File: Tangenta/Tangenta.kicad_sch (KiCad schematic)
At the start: 9 parts

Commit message: Improving SDcard placement and routing
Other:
- note added: "GPIOs/IOs CMOS (Flash) FANs Reset/Power pins and buttons CR2032 & RTC"
- note removed: "GPIOs/IOs CMOS (Flash) FANs Reset/Power pins and buttons CR2032, RTC & Battery"
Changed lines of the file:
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@@
     (stroke (width 0) (type default))
   )
-  (bus (pts (xy 207.01 210.185) (xy 401.955 210.185))
+  (bus (pts (xy 207.01 213.36) (xy 401.955 213.36))
     (stroke (width 0) (type default))
   )
@@
     (stroke (width 0) (type default))
   )
-  (bus (pts (xy 207.01 205.105) (xy 207.01 210.185))
+  (bus (pts (xy 207.01 205.105) (xy 207.01 213.36))
     (stroke (width 0) (type default))
   )
@@
     (stroke (width 0) (type default))
   )
-  (bus (pts (xy 401.955 210.185) (xy 401.955 125.73))
+  (bus (pts (xy 401.955 213.36) (xy 401.955 125.73))
     (stroke (width 0) (type default))
   )
@@
     (stroke (width 0) (type default))
   )
-  (text "GPIOs/IOs\n\nCMOS (Flash)\n\nFANs\n\nReset/Power pins\nand buttons\n\nCR2032, RTC & Battery"
+  (text "GPIOs/IOs\n\nCMOS (Flash)\n\nFANs\n\nReset/Power pins\nand buttons\n\nCR2032 & RTC"
     (at -100.965 160.655 0)
     (effects (font (size 5 5)) (justify left bottom))

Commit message: RTC continued...
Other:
- added sheet RTC (RTC.kicad_sch)
- note added: "GPIOs/IOs CMOS (Flash) FANs Reset/Power pins and buttons"
- note removed: "GPIOs/IOs CMOS (Flash) FANs Reset/Power pins and buttons CR2032 & RTC"
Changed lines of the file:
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@@
   (junction (at 278.765 150.495) (diameter 0) (color 0 0 0 0)
+  )
+  (junction (at 207.01 213.36) (diameter 0) (color 0 0 0 0)
   )
   (junction (at 207.01 205.105) (diameter 0) (color 0 0 0 0)
@@
     (stroke (width 0) (type default))
   )
+  (wire (pts (xy 241.3 225.425) (xy 254.635 225.425))
+    (stroke (width 0) (type default))
+  )
   (wire (pts (xy 254.635 133.35) (xy 267.97 133.35))
     (stroke (width 0) (type default))
@@
     (stroke (width 0) (type default))
   )
+  (bus (pts (xy 207.01 231.14) (xy 207.01 213.36))
+    (stroke (width 0) (type default))
+  )
   (wire (pts (xy 355.6 150.495) (xy 368.935 150.495))
     (stroke (width 0) (type default))
   )
+  (wire (pts (xy 241.3 222.885) (xy 254.635 222.885))
+    (stroke (width 0) (type default))
+  )
   (wire (pts (xy 333.375 187.325) (xy 346.71 187.325))
     (stroke (width 0) (type default))
@@
     (stroke (width 0) (type default))
   )
+  (bus (pts (xy 214.63 231.14) (xy 207.01 231.14))
+    (stroke (width 0) (type default))
+  )
   (bus (pts (xy 401.955 213.36) (xy 401.955 125.73))
     (stroke (width 0) (type default))
@@
     (stroke (width 0) (type default))
   )
-  (text "GPIOs/IOs\n\nCMOS (Flash)\n\nFANs\n\nReset/Power pins\nand buttons\n\nCR2032 & RTC"
+  (text "GPIOs/IOs\n\nCMOS (Flash)\n\nFANs\n\nReset/Power pins\nand buttons"
     (at -100.965 160.655 0)
     (effects (font (size 5 5)) (justify left bottom))
@@
     (effects (font (size 1.27 1.27)) (justify right bottom))
   )
+  (label "GND" (at 254.635 225.425 180) (fields_autoplaced)
+    (effects (font (size 1.27 1.27)) (justify right bottom))
+  )
   (label "GND" (at 402.59 52.07 180) (fields_autoplaced)
     (effects (font (size 1.27 1.27)) (justify right bottom))
@@
   )
   (label "GND" (at 346.71 147.955 180) (fields_autoplaced)
+    (effects (font (size 1.27 1.27)) (justify right bottom))
+  )
+  (label "3V3" (at 254.635 222.885 180) (fields_autoplaced)
     (effects (font (size 1.27 1.27)) (justify right bottom))
   )
@@
       )
     )
+  )
+  (sheet (at 214.63 219.71) (size 26.67 17.145) (fields_autoplaced)
+    (stroke (width 0.1524) (type solid))
+    (fill (color 0 0 0 0.0000))
+    (property "Sheetname" "RTC" (at 214.63 218.9984 0)
+      (effects (font (size 1.27 1.27)) (justify left bottom))
+    )
+    (property "Sheetfile" "RTC.kicad_sch" (at 214.63 237.4396 0)
+      (effects (font (size 1.27 1.27)) (justify left top))
+    )
+    (pin "SMBUS{SCL SDA}" input (at 214.63 231.14 180)
+      (effects (font (size 1.27 1.27)) (justify left))
+    )
+    (pin "3V3" input (at 241.3 222.885 0)
+      (effects (font (size 1.27 1.27)) (justify right))
+    )
+    (pin "GND" bidirectional (at 241.3 225.425 0)
+      (effects (font (size 1.27 1.27)) (justify right))
+    )
+    (instances
+      (project "Tangenta"
+        (path "/358d1bcf-7599-4352-8c4d-baa18a5f09e6" (page "28"))
+      )
+    )

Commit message: DualCMOS
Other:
- added sheet DualCMOS (DualCMOS.kicad_sch)
- note added: "GPIOs/IOs FANs Reset/Power pins and buttons"
- note removed: "GPIOs/IOs CMOS (Flash) FANs Reset/Power pins and buttons"
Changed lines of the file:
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@@
   (junction (at 278.765 150.495) (diameter 0) (color 0 0 0 0)
+  )
+  (junction (at 207.01 231.14) (diameter 0) (color 0 0 0 0)
   )
   (junction (at 207.01 213.36) (diameter 0) (color 0 0 0 0)
@@
     (stroke (width 0) (type default))
   )
+  (wire (pts (xy 241.3 249.555) (xy 254.635 249.555))
+    (stroke (width 0) (type default))
+  )
   (bus (pts (xy 188.595 170.815) (xy 294.64 170.815))
     (stroke (width 0) (type default))
@@
     (stroke (width 0) (type default))
   )
+  (bus (pts (xy 214.63 249.555) (xy 207.01 249.555))
+    (stroke (width 0) (type default))
+  )
   (wire (pts (xy 46.355 171.45) (xy 52.705 171.45))
     (stroke (width 0) (type default))
@@
     (stroke (width 0) (type default))
   )
+  (wire (pts (xy 241.3 247.015) (xy 254.635 247.015))
+    (stroke (width 0) (type default))
+  )
   (wire (pts (xy 85.09 159.385) (xy 98.425 159.385))
     (stroke (width 0) (type default))
@@
     (stroke (width 0) (type default))
   )
+  (bus (pts (xy 207.01 249.555) (xy 207.01 231.14))
+    (stroke (width 0) (type default))
+  )
   (wire (pts (xy 254.635 135.89) (xy 267.97 135.89))
     (stroke (width 0) (type default))
@@
     (stroke (width 0) (type default))
   )
-  (text "GPIOs/IOs\n\nCMOS (Flash)\n\nFANs\n\nReset/Power pins\nand buttons"
-    (at -100.965 160.655 0)
+  (text "GPIOs/IOs\n\nFANs\n\nReset/Power pins\nand buttons" (at -100.965 160.655 0)
     (effects (font (size 5 5)) (justify left bottom))
   )
@@
   )
   (label "1V8" (at 98.425 90.805 180) (fields_autoplaced)
+    (effects (font (size 1.27 1.27)) (justify right bottom))
+  )
+  (label "GND" (at 254.635 249.555 180) (fields_autoplaced)
     (effects (font (size 1.27 1.27)) (justify right bottom))
   )
@@
   )
   (label "CHASSIS" (at 346.71 189.865 180) (fields_autoplaced)
+    (effects (font (size 1.27 1.27)) (justify right bottom))
+  )
+  (label "3V3" (at 254.635 247.015 180) (fields_autoplaced)
     (effects (font (size 1.27 1.27)) (justify right bottom))
   )
@@
       )
     )
+  )
+  (sheet (at 214.63 243.84) (size 26.67 16.51) (fields_autoplaced)
+    (stroke (width 0.1524) (type solid))
+    (fill (color 0 0 0 0.0000))
+    (property "Sheetname" "DualCMOS" (at 214.63 243.1284 0)
+      (effects (font (size 1.27 1.27)) (justify left bottom))
+    )
+    (property "Sheetfile" "DualCMOS.kicad_sch" (at 214.63 260.9346 0)
+      (effects (font (size 1.27 1.27)) (justify left top))
+    )
+    (pin "SMBUS{SCL SDA}" input (at 214.63 249.555 180)
+      (effects (font (size 1.27 1.27)) (justify left))
+    )
+    (pin "GND" bidirectional (at 241.3 249.555 0)
+      (effects (font (size 1.27 1.27)) (justify right))
+    )
+    (pin "3V3" input (at 241.3 247.015 0)
+      (effects (font (size 1.27 1.27)) (justify right))
+    )
+    (instances
+      (project "Tangenta"
+        (path "/358d1bcf-7599-4352-8c4d-baa18a5f09e6" (page "29"))
+      )
+    )

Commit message: Adding on-board PWR and RST tactile buttons.
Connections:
- no-connect marks 2 -> 0
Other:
- sheet Toradex ports: added PWR, RST; removed none
- note added: "JTAG GPIOs/IOs FANs ADC"
- note removed: "GPIOs/IOs FANs Reset/Power pins and buttons"
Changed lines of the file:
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@@
   (junction (at 207.01 205.105) (diameter 0) (color 0 0 0 0)
   )
-  (no_connect (at 295.91 31.75))
-  (no_connect (at 295.91 34.29))
   (wire (pts (xy 389.255 34.29) (xy 402.59 34.29))
     (stroke (width 0) (type default))
@@
     (stroke (width 0) (type default))
   )
+  (wire (pts (xy 188.595 31.75) (xy 300.355 31.75))
+    (stroke (width 0) (type default))
+  )
   (wire (pts (xy 107.315 24.765) (xy 93.98 24.765))
     (stroke (width 0) (type default))
@@
     (stroke (width 0) (type default))
   )
-  (wire (pts (xy 295.91 34.29) (xy 300.355 34.29))
-    (stroke (width 0) (type default))
-  )
   (wire (pts (xy 368.935 147.955) (xy 355.6 147.955))
     (stroke (width 0) (type default))
@@
     (stroke (width 0) (type default))
   )
-  (wire (pts (xy 295.91 31.75) (xy 300.355 31.75))
-    (stroke (width 0) (type default))
-  )
   (bus (pts (xy 188.595 161.29) (xy 294.64 161.29))
     (stroke (width 0) (type default))
@@
     (stroke (width 0) (type default))
   )
+  (wire (pts (xy 188.595 34.29) (xy 300.355 34.29))
+    (stroke (width 0) (type default))
+  )
   (bus (pts (xy 188.595 95.25) (xy 214.63 95.25))
     (stroke (width 0) (type default))
   )
-  (text "GPIOs/IOs\n\nFANs\n\nReset/Power pins\nand buttons" (at -100.965 160.655 0)
+  (text "JTAG\n\nGPIOs/IOs\n\nFANs\n\nADC" (at -100.965 160.655 0)
     (effects (font (size 5 5)) (justify left bottom))
   )
@@
       (effects (font (size 1.27 1.27)) (justify right))
     )
+    (pin "PWR" input (at 188.595 34.29 0)
+      (effects (font (size 1.27 1.27)) (justify right))
+    )
+    (pin "RST" input (at 188.595 31.75 0)
+      (effects (font (size 1.27 1.27)) (justify right))
+    )

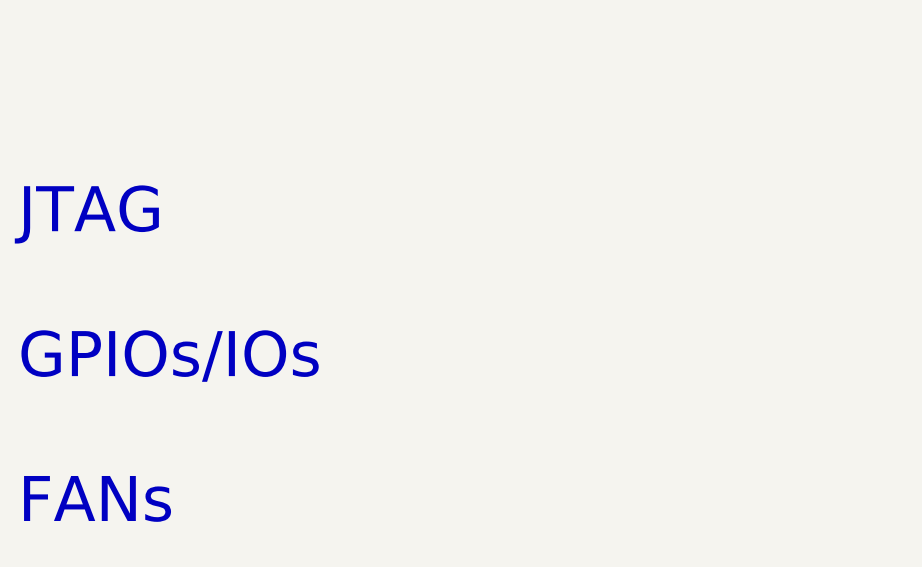
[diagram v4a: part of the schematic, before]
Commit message: Adding a hint about recovery jumper.
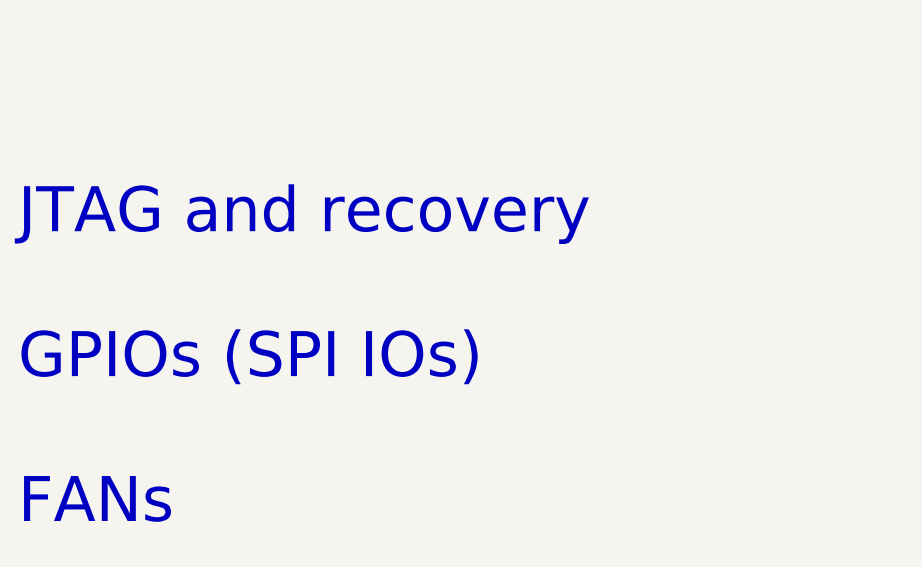
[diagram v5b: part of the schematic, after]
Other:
- note added: "JTAG and recovery GPIOs (SPI IOs) FANs ADC"
- note removed: "JTAG GPIOs/IOs FANs ADC"
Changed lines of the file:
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@@
     (stroke (width 0) (type default))
   )
-  (text "JTAG\n\nGPIOs/IOs\n\nFANs\n\nADC" (at -100.965 160.655 0)
+  (text "JTAG and recovery\n\nGPIOs (SPI IOs)\n\nFANs\n\nADC" (at -100.965 160.655 0)
     (effects (font (size 5 5)) (justify left bottom))
   )

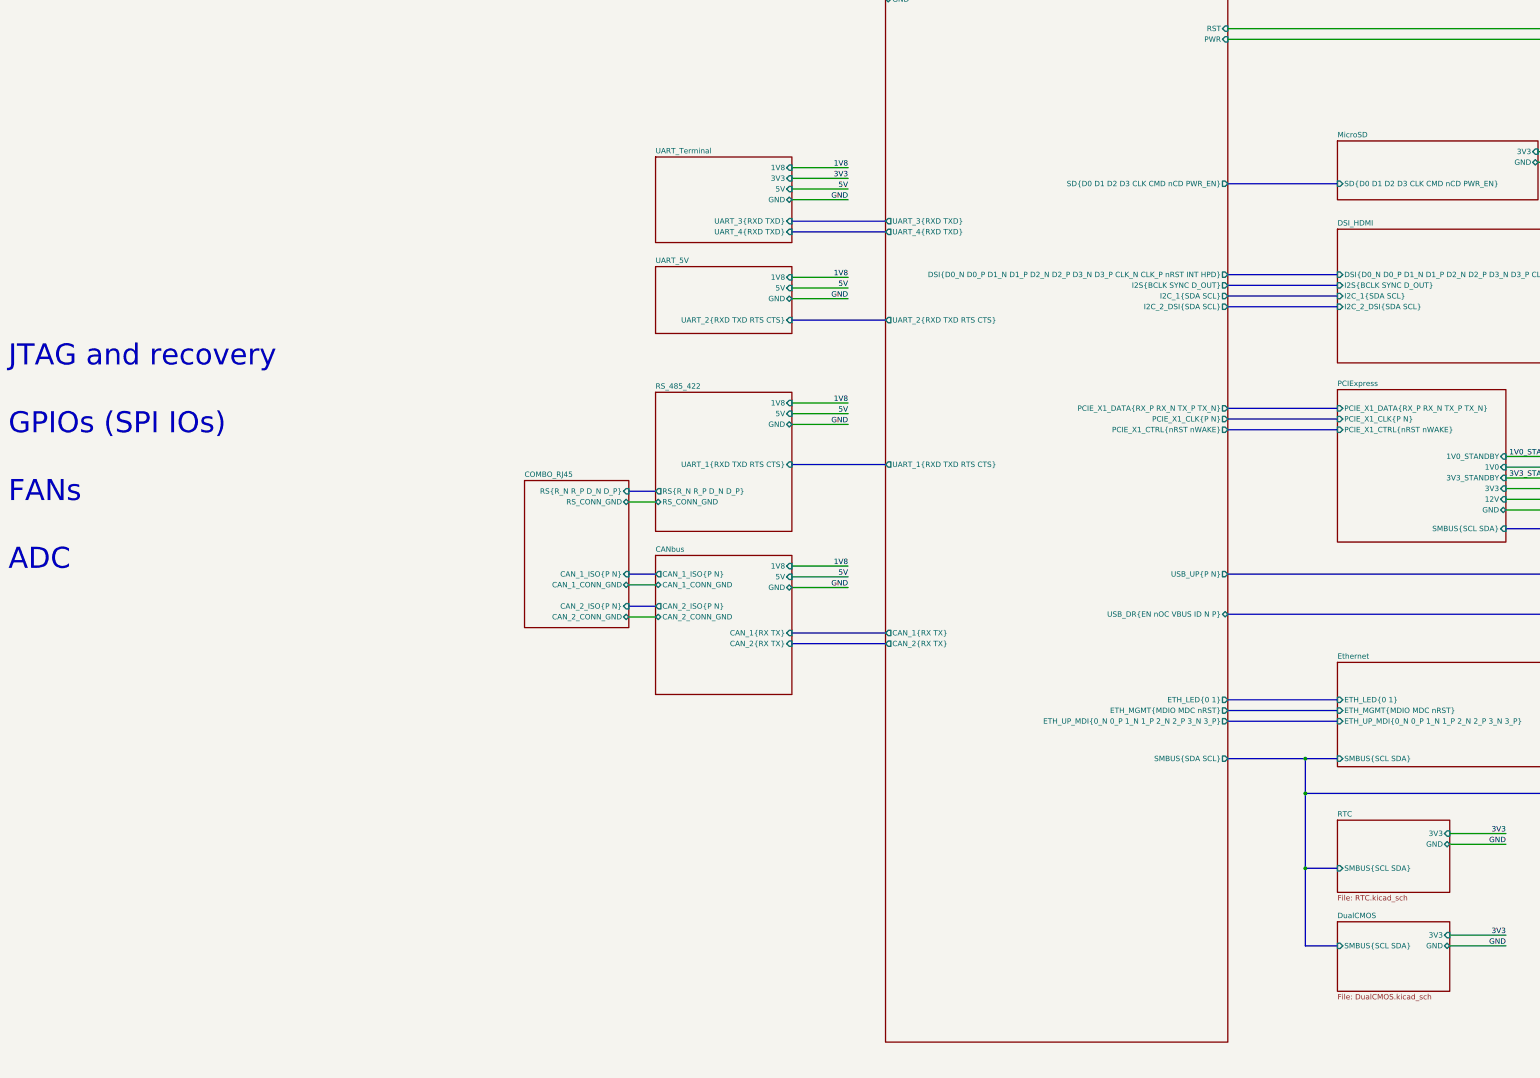
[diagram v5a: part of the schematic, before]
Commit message: Adding JTAG.
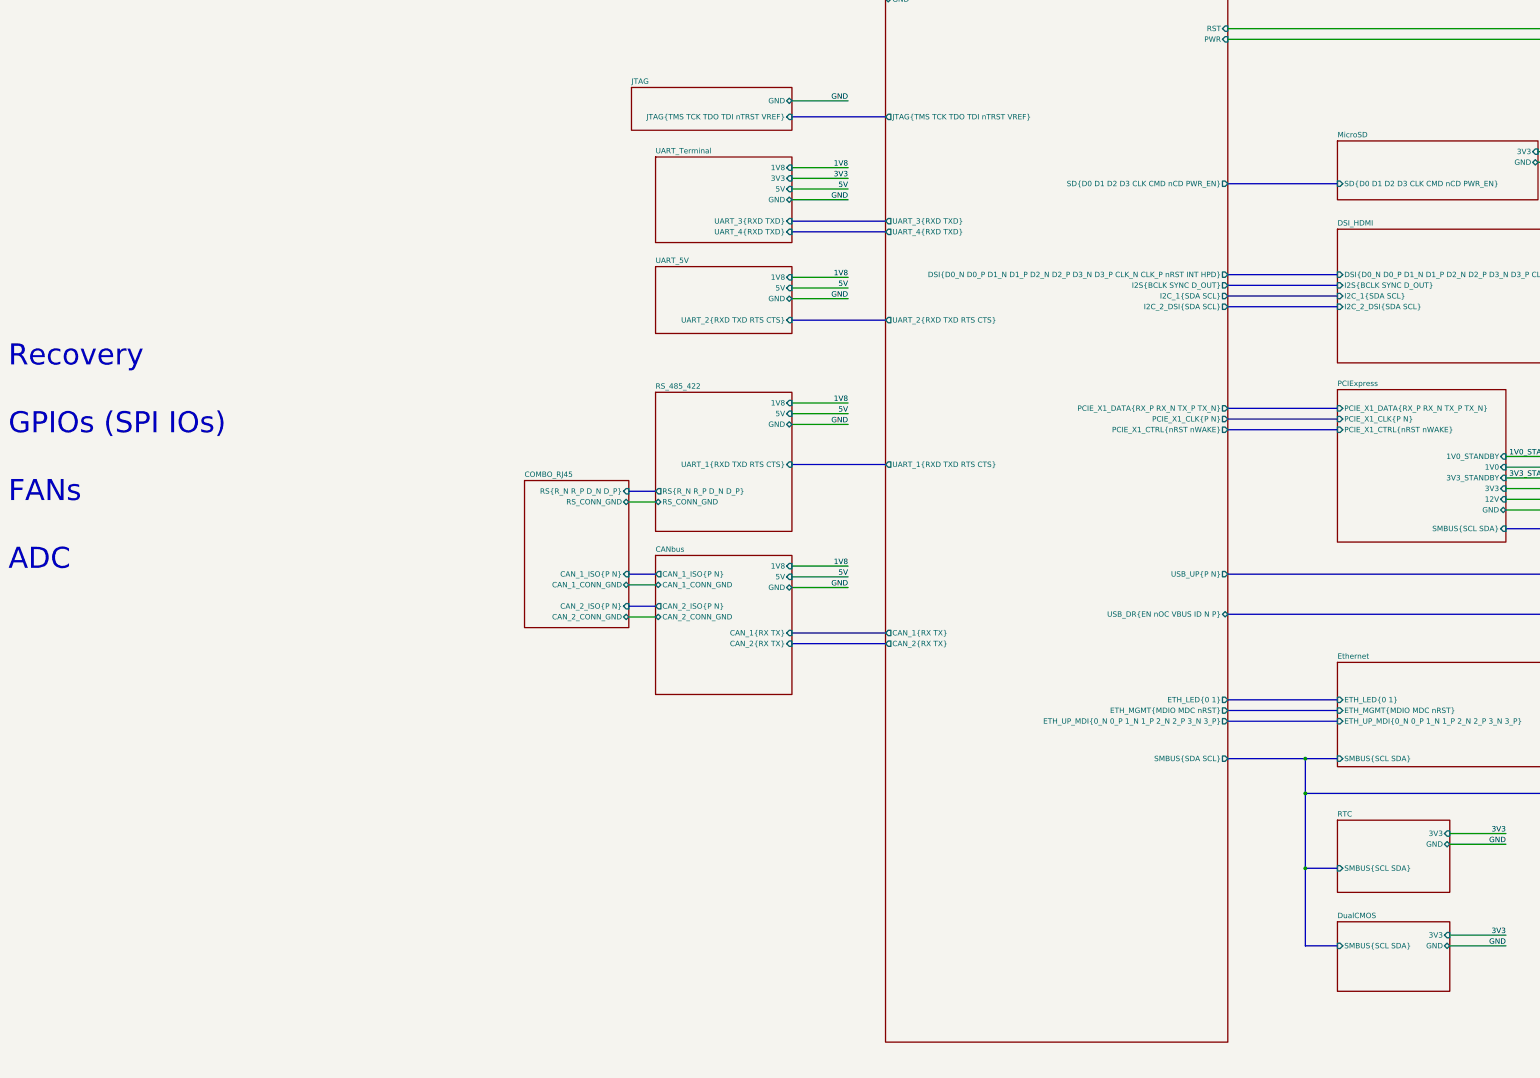
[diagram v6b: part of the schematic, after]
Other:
- added sheet JTAG (JTAG.kicad_sch)
- sheet Toradex ports: added JTAG{TMS TCK TDO TDI nTRST VREF}; removed none
- note added: "Recovery GPIOs (SPI IOs) FANs ADC"
- note removed: "JTAG and recovery GPIOs (SPI IOs) FANs ADC"
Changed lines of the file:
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@@
+    (stroke (width 0) (type default))
+  )
+  (bus (pts (xy 85.09 52.705) (xy 107.315 52.705))
     (stroke (width 0) (type default))
   )
@@
     (stroke (width 0) (type default))
   )
+  (wire (pts (xy 85.09 48.895) (xy 98.425 48.895))
+    (stroke (width 0) (type default))
+  )
   (bus (pts (xy 188.595 161.29) (xy 294.64 161.29))
     (stroke (width 0) (type default))
@@
     (stroke (width 0) (type default))
   )
-  (text "JTAG and recovery\n\nGPIOs (SPI IOs)\n\nFANs\n\nADC" (at -100.965 160.655 0)
+  (text "Recovery\n\nGPIOs (SPI IOs)\n\nFANs\n\nADC" (at -100.965 160.655 0)
     (effects (font (size 5 5)) (justify left bottom))
   )
@@
   )
   (label "GND" (at 98.425 72.39 180) (fields_autoplaced)
+    (effects (font (size 1.27 1.27)) (justify right bottom))
+  )
+  (label "GND" (at 98.425 48.895 180) (fields_autoplaced)
     (effects (font (size 1.27 1.27)) (justify right bottom))
   )
@@
     )
     (property "Sheetfile" "RTC.kicad_sch" (at 214.63 237.4396 0)
-      (effects (font (size 1.27 1.27)) (justify left top))
+      (effects (font (size 1.27 1.27)) (justify left top) hide)
     )
     (pin "SMBUS{SCL SDA}" input (at 214.63 231.14 180)
@@
     )
     (property "Sheetfile" "DualCMOS.kicad_sch" (at 214.63 260.9346 0)
-      (effects (font (size 1.27 1.27)) (justify left top))
+      (effects (font (size 1.27 1.27)) (justify left top) hide)
     )
     (pin "SMBUS{SCL SDA}" input (at 214.63 249.555 180)
@@
     )
   )
+  (sheet (at 46.99 45.72) (size 38.1 10.16) (fields_autoplaced)
+    (stroke (width 0.1524) (type solid))
+    (fill (color 0 0 0 0.0000))
+    (property "Sheetname" "JTAG" (at 46.99 45.0084 0)
+      (effects (font (size 1.27 1.27)) (justify left bottom))
+    )
+    (property "Sheetfile" "JTAG.kicad_sch" (at 46.99 56.4646 0)
+      (effects (font (size 1.27 1.27)) (justify left top) hide)
+    )
+    (pin "JTAG{TMS TCK TDO TDI nTRST VREF}" input (at 85.09 52.705 0)
+      (effects (font (size 1.27 1.27)) (justify right))
+    )
+    (pin "GND" bidirectional (at 85.09 48.895 0)
+      (effects (font (size 1.27 1.27)) (justify right))
+    )
+    (instances
+      (project "Tangenta"
+        (path "/358d1bcf-7599-4352-8c4d-baa18a5f09e6" (page "30"))
+      )
+    )
+  )
   (sheet (at 52.705 118.11) (size 32.385 33.02) (fields_autoplaced)
     (stroke (width 0.1524) (type solid))
@@
       (effects (font (size 1.27 1.27)) (justify right))
     )
-    (instances
+    (pin "JTAG{TMS TCK TDO TDI nTRST VREF}" output (at 107.315 52.705 180)
+      (effects (font (size 1.27 1.27)) (justify left))
+    )
+    (instances
